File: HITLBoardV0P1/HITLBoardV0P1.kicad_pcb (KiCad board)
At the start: 2 copper layers, 199 parts, among them J2 FTSH-105-01-L-DV, U1 TMDX570LC43HDK_Connectors, U10 DAC7750IPWPR, U11 NC7SZ04P5X, U12 SN74LVC1G08DCKR, U13 NC7SZ04P5X, U14 SN74LVC1G08DCKR, U15 DAC7750IPWPR, U16 NC7SZ04P5X, U17 SN74LVC1G08DCKR, U18 DAC7750IPWPR, U19 NC7SZ04P5X, U2 LAN8650B1-E/LMX, U20 SN74LVC1G08DCKR, U21 DAC7750IPWPR, U3 LP38852MRX-ADJ/NOPB, U4 LAN8650B1-E/LMX, U5 LP38852MRX-ADJ/NOPB, U6 LAN8650B1-E/LMX, U7 LP38852MRX-ADJ/NOPB, U8 LAN8650B1-E/LMX, U9 LP38852MRX-ADJ/NOPB

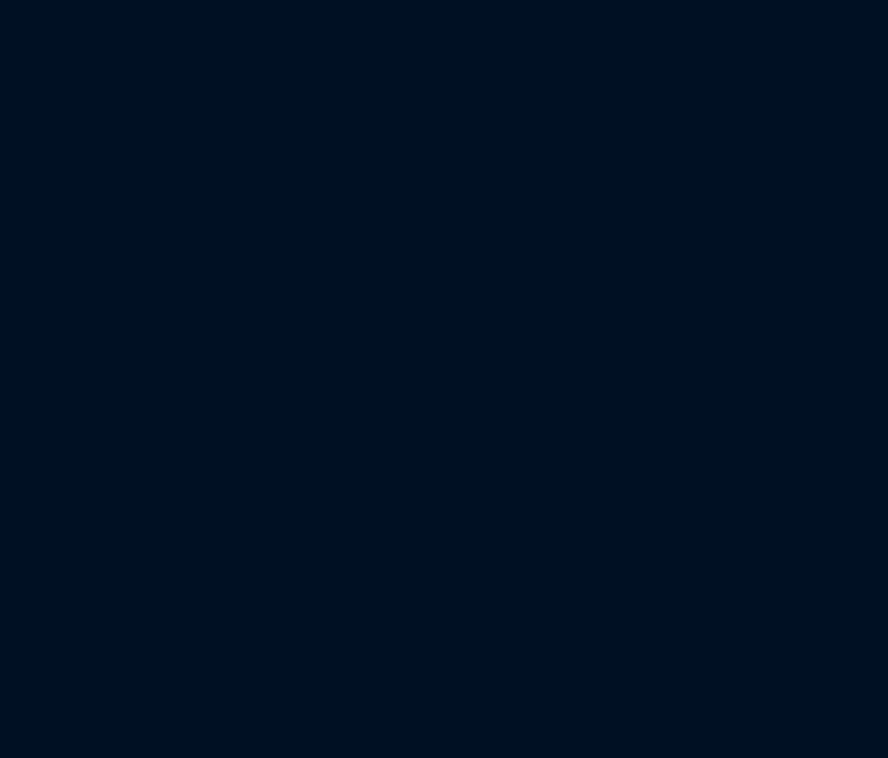
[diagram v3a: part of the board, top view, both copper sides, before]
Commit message: update to board with spi buses assigned
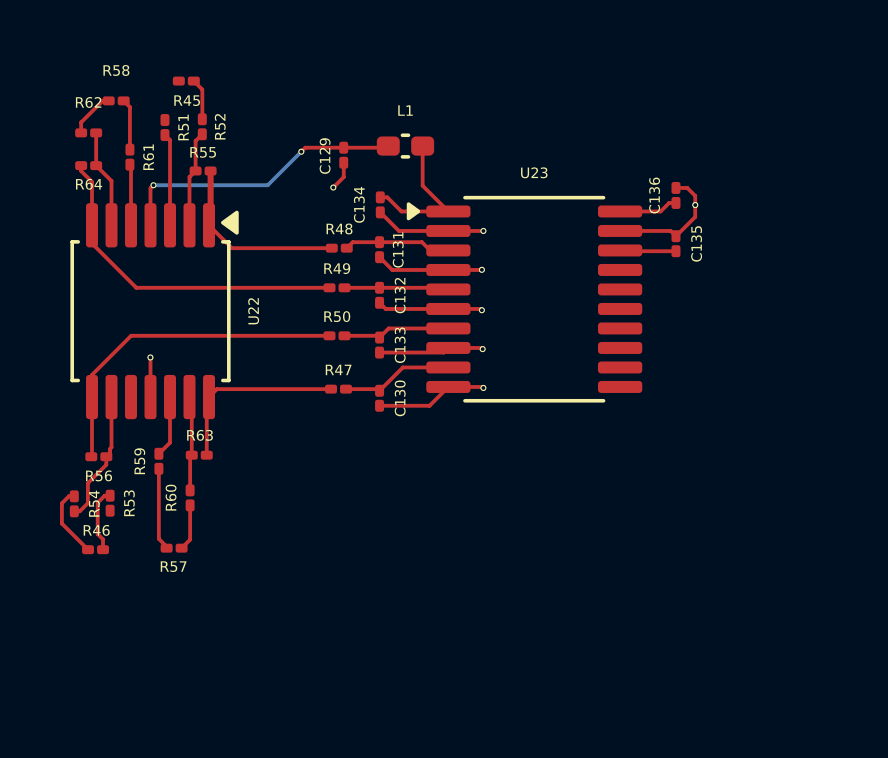
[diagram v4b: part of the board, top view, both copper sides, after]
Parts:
- added C129: C_Small, Capacitor_SMD:C_01005_0402Metric, F.Cu at (84.0, 37.9)
- added C130: C_Small, Capacitor_SMD:C_01005_0402Metric, F.Cu at (85.2, 46.0)
- added C131: C_Small, Capacitor_SMD:C_01005_0402Metric, F.Cu at (85.2, 41.0)
- added C132: C_Small, Capacitor_SMD:C_01005_0402Metric, F.Cu at (85.2, 42.5)
- added C133: C_Small, Capacitor_SMD:C_01005_0402Metric, F.Cu at (85.2, 44.2)
- added C134: C_Small, Capacitor_SMD:C_01005_0402Metric, F.Cu at (85.3, 39.5)
- added C135: C_Small, Capacitor_SMD:C_01005_0402Metric, F.Cu at (95.1, 40.8)
- added C136: C_Small, Capacitor_SMD:C_01005_0402Metric, F.Cu at (95.1, 39.2)
- added L1: L_Ferrite, Inductor_SMD:L_0402_1005Metric_Pad0.77x0.64mm_HandSolder, F.Cu at (86.1, 37.6)
- added R45: 150, Resistor_SMD:R_01005_0402Metric, F.Cu at (78.8, 35.4)
- added R46: 150, Resistor_SMD:R_01005_0402Metric, F.Cu at (75.8, 51.0)
- added R47: R_US, Resistor_SMD:R_01005_0402Metric, F.Cu at (83.9, 45.7)
- added R48: R_US, Resistor_SMD:R_01005_0402Metric, F.Cu at (83.9, 41.0)
- added R49: R_US, Resistor_SMD:R_01005_0402Metric, F.Cu at (83.8, 42.3)
- added R50: R_US, Resistor_SMD:R_01005_0402Metric, F.Cu at (83.8, 43.9)
- added R51: 1K, Resistor_SMD:R_01005_0402Metric, F.Cu at (78.1, 36.9)
- added R52: 1K, Resistor_SMD:R_01005_0402Metric, F.Cu at (79.3, 36.9)
- added R53: 100K, Resistor_SMD:R_01005_0402Metric, F.Cu at (76.3, 49.5)
- added R54: 100K, Resistor_SMD:R_01005_0402Metric, F.Cu at (75.1, 49.5)
- added R55: 1K, Resistor_SMD:R_01005_0402Metric, F.Cu at (79.4, 38.4)
- added R56: 100K, Resistor_SMD:R_01005_0402Metric, F.Cu at (75.9, 47.9)
- added R57: 150, Resistor_SMD:R_01005_0402Metric, F.Cu at (78.4, 51.0)
- added R58: 150, Resistor_SMD:R_01005_0402Metric, F.Cu at (76.5, 36.1)
- added R59: 100K, Resistor_SMD:R_01005_0402Metric, F.Cu at (77.9, 48.1)
- added R60: 100K, Resistor_SMD:R_01005_0402Metric, F.Cu at (78.9, 49.3)
- added R61: 100K, Resistor_SMD:R_01005_0402Metric, F.Cu at (76.9, 37.9)
- added R62: 100K, Resistor_SMD:R_01005_0402Metric, F.Cu at (75.5, 37.1)
- added R63: 100K, Resistor_SMD:R_01005_0402Metric, F.Cu at (79.2, 47.9)
- added R64: 100K, Resistor_SMD:R_01005_0402Metric, F.Cu at (75.5, 38.2)
- added U22: TLV4387PWR, Package_SO:TSSOP-14_4.4x5mm_P0.65mm, F.Cu at (77.6, 43.1)
- added U23: ADS131M04QPWRQ1, Package_SO:TSSOP-20_4.4x6.5mm_P0.65mm, F.Cu at (90.4, 42.7)
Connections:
- U10 pad 10: /DAC/SDO -> /RPI_SPI1_MISO
- U10 pad 6: /DAC/CLR -> /DAC_CLR0
- U10 pad 7: /DAC/LATCH -> /DAC_LATCH0
- U10 pad 9: /DAC/DIN -> /RPI_SPI1_MOSI
- U11 pad 2: /DAC/LATCH -> /DAC_LATCH0
- U12 pad 2: /DAC/SCLK -> /RPI_SPI1_SCK
- U13 pad 2: /dac2/LATCH -> /DAC_LATCH1
- U15 pad 10: /dac2/SDO -> /RPI_SPI1_MISO
- U15 pad 6: /dac2/CLR -> /DAC_CLR1
- U15 pad 7: /dac2/LATCH -> /DAC_LATCH1
- U15 pad 9: /dac2/DIN -> /RPI_SPI1_MOSI
- U16 pad 2: /dac3/LATCH -> /DAC_LATCH2
- U17 pad 2: /dac3/SCLK -> /RPI_SPI1_SCK
- U18 pad 10: /dac3/SDO -> /RPI_SPI1_MISO
- U18 pad 6: /dac3/CLR -> /DAC_CLR2
- U18 pad 7: /dac3/LATCH -> /DAC_LATCH2
- U18 pad 9: /dac3/DIN -> /RPI_SPI1_MOSI
- U19 pad 2: /dac4/LATCH -> /DAC_LATCH3
- U20 pad 2: /dac4/SCLK -> /RPI_SPI1_SCK
- U21 pad 10: /dac4/SDO -> /RPI_SPI1_MISO
- U21 pad 6: /dac4/CLR -> /DAC_CLR3
- U21 pad 7: /dac4/LATCH -> /DAC_LATCH3
- U21 pad 9: /dac4/DIN -> /RPI_SPI1_MOSI
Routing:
- net GND: track 240.0 -> 264.6 mm, vias 78 -> 86
- net /dac4/LATCH: track 20.3 -> 0.00 mm
- net /DAC_LATCH3: track 0.00 -> 20.3 mm
- net /dac2/LATCH: track 16.8 -> 0.00 mm, vias 2 -> 0
- net /DAC_LATCH1: track 0.00 -> 16.8 mm, vias 0 -> 2
- net /dac3/LATCH: track 16.0 -> 0.00 mm, vias 2 -> 0
- net /DAC_LATCH2: track 0.00 -> 16.0 mm, vias 0 -> 2
- net /DAC_LATCH0: track 0.00 -> 14.6 mm, vias 0 -> 2
- net /DAC/LATCH: track 14.6 -> 0.00 mm, vias 2 -> 0
- net /CurrentInstrument/Out_B: track 0.00 -> 11.3 mm
- net /CurrentInstrument/Out_C: track 0.00 -> 11.2 mm
- net +3V3: track 141.3 -> 151.1 mm, vias 24 -> 26
- net /CurrentInstrument/Out_A: track 0.00 -> 6.32 mm
- net /CurrentInstrument/Out_D: track 0.00 -> 6.15 mm
- net Net-(U23-AVDD): track 0.00 -> 5.00 mm
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
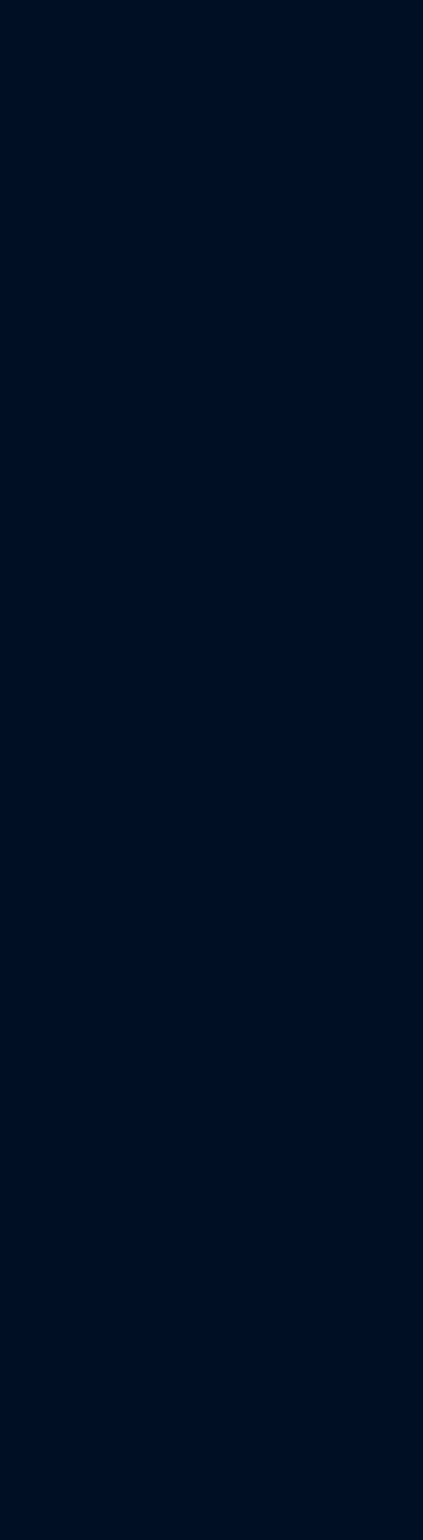
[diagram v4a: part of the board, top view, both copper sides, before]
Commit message: ADD SOLENOID VALVE CIRCUIT
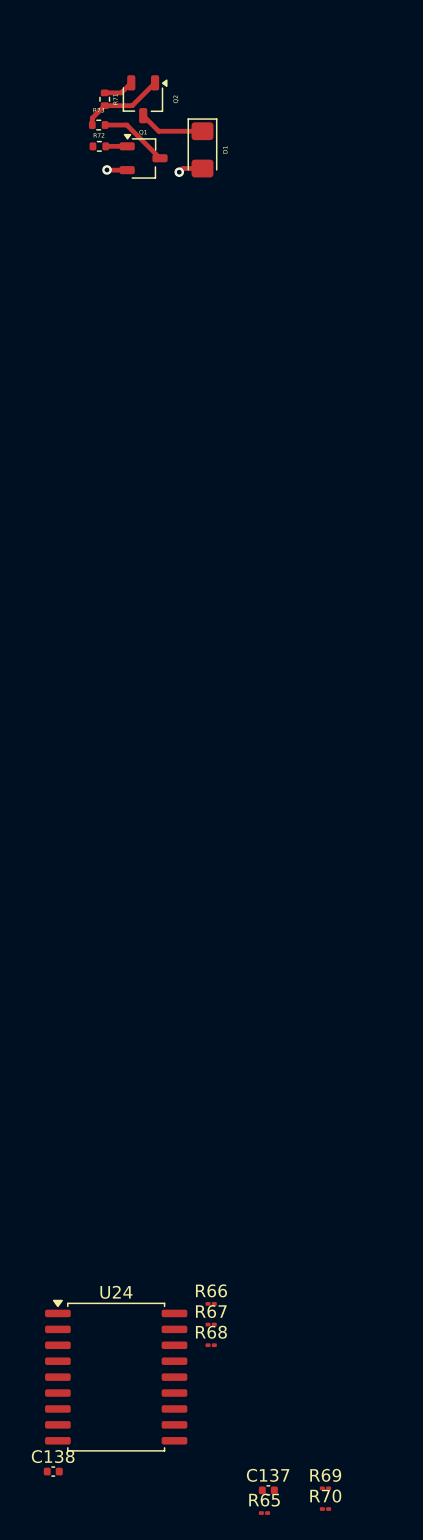
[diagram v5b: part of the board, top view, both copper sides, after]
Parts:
- added C137: 0.1u, Capacitor_SMD:C_0402_1005Metric, F.Cu at (70.6, 228.8)
- added C138: 0.1u, Capacitor_SMD:C_0402_1005Metric, F.Cu at (53.4, 227.3)
- added D1: D_Schottky, Diode_SMD:D_1206_3216Metric_Pad1.42x1.75mm_HandSolder, F.Cu at (65.3, 121.8)
- added Q1: NPN, GaladyneFootprintsLibrary:TSOT-23_KSC1623GMTF, F.Cu at (60.6, 122.5)
- added Q2: PMOS, GaladyneFootprintsLibrary:TSOT-23_ZXMP6A14FQ, F.Cu at (60.6, 117.8)
- added R65: 10K, Resistor_SMD:R_01005_0402Metric, F.Cu at (70.3, 230.6)
- added R66: 10K, Resistor_SMD:R_01005_0402Metric, F.Cu at (66.0, 213.9)
- added R67: 10K, Resistor_SMD:R_01005_0402Metric, F.Cu at (66.0, 215.6)
- added R68: 10K, Resistor_SMD:R_01005_0402Metric, F.Cu at (66.0, 217.2)
- added R69: 10K, Resistor_SMD:R_01005_0402Metric, F.Cu at (75.2, 228.6)
- added R70: 10K, Resistor_SMD:R_01005_0402Metric, F.Cu at (75.2, 230.3)
- added R71: 10K, Resistor_SMD:R_0402_1005Metric, F.Cu at (57.5, 117.8)
- added R72: 33, Resistor_SMD:R_0402_1005Metric, F.Cu at (57.1, 121.6)
- added R73: 4.7K, Resistor_SMD:R_0402_1005Metric, F.Cu at (57.1, 119.9)
- added U24: MCP23008-E/SO, Package_SO:SOIC-18W_7.5x11.6mm_P1.27mm, F.Cu at (58.5, 219.8)
- C129, C131, C132, C133, C134, C136: value C_Small -> 0.1u
- C130, C135: value C_Small -> 0.1U
- R47, R48, R49, R50: value R_US -> 500
- R51, R52: value 1K -> 100K
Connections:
- A1 pad 31: /LAN_RESET_N_1 -> /RPI_I2C_SDA
- A1 pad 32: /LAN_WAKE_0 -> /RPI_I2C_SCL
- A1 pad 34: /LAN_WAKE_1 -> /GPIO_XPNDR_IRQ
- C107 pad 1: /DAC/CURRENT_OUT -> /I_LOOP_1
- C114 pad 1: /dac2/CURRENT_OUT -> /I_LOOP_2
- C121 pad 1: /dac3/CURRENT_OUT -> /I_LOOP_3
- C128 pad 1: /dac4/CURRENT_OUT -> /I_LOOP_4
- R2 pad 1: /Ethernet/RESET_N -> /LAN1_RESET_N
- R26 pad 1: /ethernet4/RESET_N -> /LAN2_RESET_N
- R27 pad 1: /ethernet4/IRQ_N -> /LAN2_IRQ_N
- R3 pad 1: /Ethernet/IRQ_N -> /LAN1_IRQ_N
- R34 pad 2: /DAC/CURRENT_OUT -> /I_LOOP_1
- R38 pad 2: /dac2/CURRENT_OUT -> /I_LOOP_2
- R41 pad 2: /dac3/CURRENT_OUT -> /I_LOOP_3
- R44 pad 2: /dac4/CURRENT_OUT -> /I_LOOP_4
- R45 pad 2: Net-(R45-Pad2) -> /I_LOOP_1
- R46 pad 2: Net-(R46-Pad2) -> /I_LOOP_3
- R51 pad 1: Net-(R45-Pad2) -> /I_LOOP_1
- R53 pad 1: Net-(R46-Pad2) -> /I_LOOP_3
- R57 pad 2: Net-(R57-Pad2) -> /I_LOOP_4
- R58 pad 2: Net-(R58-Pad2) -> /I_LOOP_2
- R59 pad 1: Net-(R57-Pad2) -> /I_LOOP_4
- R61 pad 1: Net-(R58-Pad2) -> /I_LOOP_2
- U1 pad P11-19: /TMDX_Breakout/GIOA_1 -> /LAN1_WAKE
- U1 pad P11-21: /TMDX_Breakout/GIOA_3 -> /LAN2_WAKE
- U1 pad P11-23: /TMDX_Breakout/GIOA_5 -> /LAN1_RESET_N
- U1 pad P11-25: /TMDX_Breakout/GIOA_7 -> /LAN2_RESET_N
- U1 pad P11-27: /TMDX_Breakout/GIOB_1 -> /LAN1_IRQ_N
- U1 pad P11-29: /TMDX_Breakout/GIOB_3 -> /LAN2_IRQ_N
- U1 pad P11-5: /TMDX_Breakout/SCI1_RX -> /RPI_UART1_TX
- U1 pad P11-6: /TMDX_Breakout/SCI1_TX -> /RPI_UART1_RX
- U1 pad P9-11: /TMDX_Breakout/SPI1_SIMO -> /TMDX_SPI1_SIMO
- U1 pad P9-12: /TMDX_Breakout/SPI1_SOMI -> /TMDX_SPI1_SOMI
- U1 pad P9-16: unconnected-(U1A-SPI5_CLK-PadP9-16) -> /TMDX_Breakout/SPI5_SCLK
- U1 pad P9-17: unconnected-(U1A-SPI5_CS1_N-PadP9-17) -> /TMDX_Breakout/SPI5_CS1_NR
- U1 pad P9-18: unconnected-(U1A-SPI5_CS0_N-PadP9-18) -> /TMDX_Breakout/SPI5_CS0_N
- U1 pad P9-21: unconnected-(U1A-SPI5_SIMO_0-PadP9-21) -> /TMDX_Breakout/SPI5_SIMO_0
- U1 pad P9-22: unconnected-(U1A-SPI5_SOMI_0-PadP9-22) -> /TMDX_Breakout/SPI5_SOMI_0
- U1 pad P9-6: /TMDX_Breakout/SPI1_CLK -> /TMDX_SPI1_SCLK
- U1 pad P9-7: /TMDX_Breakout/SPI1_CS1 -> /TMDX_SPI1_CS1
- U1 pad P9-8: /TMDX_Breakout/SPI1_CS0_N -> /TMDX_SPI1_CS0_N
- U2 pad 10: /Ethernet/SPI_SDO -> /TMDX_SPI1_SOMI
- U2 pad 11: /Ethernet/SPI_CS_N -> /TMDX_SPI1_CS0_N
- U2 pad 12: /Ethernet/SPI_SCLK -> /TMDX_SPI1_SCLK
- U2 pad 13: /Ethernet/SPI_SDI -> /TMDX_SPI1_SIMO
- U2 pad 32: /Ethernet/WAKE_IN_3V3 -> /LAN1_WAKE
- U2 pad 8: /Ethernet/RESET_N -> /LAN1_RESET_N
- U2 pad 9: /Ethernet/IRQ_N -> /LAN1_IRQ_N
- U23 pad 12: unconnected-(U23-CHIP_SELECT_N-Pad12) -> /ADC_CS_N
- U23 pad 13: unconnected-(U23-DATA_READY_N-Pad13) -> /ADC_DRDY
- U23 pad 14: unconnected-(U23-SCLK-Pad14) -> /CurrentInstrument/SCLK
- U23 pad 15: unconnected-(U23-DOUT-Pad15) -> /CurrentInstrument/SDO
- U23 pad 16: unconnected-(U23-DIN-Pad16) -> /CurrentInstrument/SDI
- U8 pad 10: /ethernet4/SPI_SDO -> /TMDX_SPI1_SOMI
- U8 pad 11: /ethernet4/SPI_CS_N -> /TMDX_SPI1_CS1
- U8 pad 12: /ethernet4/SPI_SCLK -> /TMDX_SPI1_SCLK
- U8 pad 13: /ethernet4/SPI_SDI -> /TMDX_SPI1_SIMO
- U8 pad 32: /ethernet4/WAKE_IN_3V3 -> /LAN2_WAKE
- U8 pad 8: /ethernet4/RESET_N -> /LAN2_RESET_N
- U8 pad 9: /ethernet4/IRQ_N -> /LAN2_IRQ_N
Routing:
- net /ethernet4/RESET_N: track 6.74 -> 0.00 mm
- net /LAN2_RESET_N: track 0.00 -> 6.74 mm
- net Net-(Q2-G): track 0.00 -> 6.73 mm
- net Net-(Q1-C): track 0.00 -> 5.48 mm
- net /Solenoid-Valve/SV_24VDC_OUT: track 0.00 -> 5.24 mm
- net /I_LOOP_4: track 0.00 -> 5.22 mm
- net /I_LOOP_3: track 0.00 -> 4.70 mm
- net /Ethernet/RESET_N: track 4.67 -> 0.00 mm
- net /Ethernet/1V8_U2: track 26.7 -> 31.4 mm
- net /I_LOOP_2: track 0.00 -> 4.31 mm
- net /Ethernet/U3_ADJ: track 3.68 -> 7.39 mm
- net /Ethernet/IRQ_N: track 3.71 -> 0.00 mm
- net GND: track 264.6 -> 268.2 mm, vias 86 -> 88
- net Net-(R57-Pad2): track 2.75 -> 0.00 mm
- net /I_LOOP_1: track 0.00 -> 2.62 mm
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
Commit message: update solenoid valve circuits
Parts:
- added D2: LED, LED_SMD:LED_01005_0402Metric, F.Cu at (69.0, 123.5)
- added D3: D_Schottky, Diode_SMD:D_1206_3216Metric_Pad1.42x1.75mm_HandSolder, F.Cu at (59.4, 178.5)
- added D4: LED, LED_SMD:LED_01005_0402Metric, F.Cu at (62.8, 179.1)
- added Q3: NPN, GaladyneFootprintsLibrary:TSOT-23_KSC1623GMTF, F.Cu at (55.4, 185.4)
- added Q4: PMOS, GaladyneFootprintsLibrary:TSOT-23_ZXMP6A14FQ, F.Cu at (53.8, 178.3)
- added R74: 500, Resistor_SMD:R_01005_0402Metric, F.Cu at (69.0, 120.3)
- added R75: 10K, Resistor_SMD:R_01005_0402Metric, F.Cu at (67.2, 120.3)
- added R76: 3500, Resistor_SMD:R_01005_0402Metric, F.Cu at (67.2, 123.5)
- added R77: 10K, Resistor_SMD:R_0402_1005Metric, F.Cu at (51.9, 182.2)
- added R78: 33, Resistor_SMD:R_0402_1005Metric, F.Cu at (51.6, 185.0)
- added R79: 4.7K, Resistor_SMD:R_0402_1005Metric, F.Cu at (56.2, 182.1)
- added R80: 500, Resistor_SMD:R_01005_0402Metric, F.Cu at (62.8, 177.3)
- added R81: 10K, Resistor_SMD:R_01005_0402Metric, F.Cu at (64.8, 177.3)
- added R82: 3500, Resistor_SMD:R_01005_0402Metric, F.Cu at (64.8, 179.1)
- moved D1 1.07 mm to (64.3, 122.0)
- moved Q2 1.07 mm to (59.6, 118.0)
- moved R73 1.07 mm to (56.0, 120.0)
- moved Q1 1.07 mm to (59.6, 122.7)
- moved R72 1.07 mm to (56.1, 121.7)
- moved R71 1.07 mm to (56.5, 118.0)
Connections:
- Q2 pad 3: /Solenoid-Valve/24VDC -> +12V
- R71 pad 1: /Solenoid-Valve/24VDC -> +12V
- R72 pad 1: /Solenoid-Valve/SV_EN_3V3 -> /SV_EN_1
- U1 pad P11-31: /TMDX_Breakout/GIOB_5 -> /SV_EN_1
- U24 pad 13: /I2C_GPIO_EXPANDER/GP3 -> /SV_ON_1
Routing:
- net /Solenoid-Valve1/SV_24VDC_OUT: track 0.00 -> 11.0 mm
- net GND: track 268.2 -> 278.1 mm, vias 88 -> 92
- net Net-(Q4-G): track 0.00 -> 6.07 mm
- net +12V: track 20.8 -> 26.6 mm, vias 0 -> 2
- net /Solenoid-Valve/SV_24VDC_OUT: track 5.24 -> 10.1 mm
- net /SV_ON_1: track 0.00 -> 3.97 mm
- net Net-(Q3-C): track 0.00 -> 3.26 mm
- net Net-(D2-A): track 0.00 -> 2.66 mm
- net Net-(Q3-B): track 0.00 -> 2.49 mm
- net /Solenoid-Valve/24VDC: track 2.45 -> 0.00 mm
- net Net-(D4-A): track 0.00 -> 1.29 mm

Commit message: add reset button groups
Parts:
- added D5: LED, LED_SMD:LED_01005_0402Metric, F.Cu at (513.6, 197.5)
- added D6: LED, LED_SMD:LED_01005_0402Metric, F.Cu at (513.6, 199.2)
- added D7: LED, LED_SMD:LED_01005_0402Metric, F.Cu at (513.6, 200.8)
- added R83: 10K, Resistor_SMD:R_01005_0402Metric, F.Cu at (487.5, 197.4)
- added R84: 10K, Resistor_SMD:R_01005_0402Metric, F.Cu at (490.2, 204.6)
- added R85: 75, Resistor_SMD:R_0402_1005Metric, F.Cu at (510.8, 197.7)
- added R86: 75, Resistor_SMD:R_0402_1005Metric, F.Cu at (510.8, 199.7)
- added R87: 75, Resistor_SMD:R_0402_1005Metric, F.Cu at (510.8, 201.7)
- added SW1: SW_Push, Button_Switch_SMD:SW_Push_1P1T_NO_E-Switch_TL3301NxxxxxG, F.Cu at (470.8, 177.8)
- added SW2: SW_Push, Button_Switch_SMD:SW_Push_1P1T_NO_E-Switch_TL3301NxxxxxG, F.Cu at (501.2, 200.5)
- moved C93 301.0 mm to (92.4, 152.6), turned to 90 degrees
- moved C90 299.3 mm to (94.2, 152.6), turned to 90 degrees
- moved C87 297.7 mm to (96.0, 152.5), turned to 90 degrees
- moved C86 296.1 mm to (97.7, 152.5), turned to 90 degrees
- moved R29 293.2 mm to (90.7, 161.7), turned to 180 degrees
- moved U9 292.2 mm to (95.0, 158.6), turned to 90 degrees
- moved R28 291.2 mm to (90.7, 163.7), turned to 180 degrees
- moved C97 290.7 mm to (99.2, 156.3), turned to -90 degrees
- moved C100 288.0 mm to (93.7, 163.9), turned to 180 degrees
- moved C78 286.6 mm to (100.4, 159.1), turned to 90 degrees
- moved C99 286.0 mm to (93.7, 165.9), turned to 180 degrees
- moved C94 285.4 mm to (96.4, 163.9), turned to 0 degrees
- moved C79 284.8 mm to (102.4, 159.1), turned to 90 degrees
- moved C76 284.0 mm to (105.2, 157.4), turned to 90 degrees
- moved C77 282.2 mm to (107.2, 157.4), turned to 90 degrees
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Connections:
- A1 pad 30: /RaspberryPiPico/RESET_N -> /RESET_N
- A1 pad TP6: unconnected-(A1-~{BOOTSEL}-PadTP6) -> /RaspberryPiPico/BOOTSEL_N
- J2 pad 10: /RaspberryPiPico/RESET_N -> /RESET_N
- R78 pad 1: /SV_EN_1 -> /SV_EN_2
- R81 pad 1: /SV_ON_1 -> /SV_ON_2
- R82 pad 2: /SV_ON_1 -> /SV_ON_2
- U1 pad P11-33: unconnected-(U1C-GIOB_7-PadP11-33) -> /SV_EN_2
- U1 pad P9-60: unconnected-(U1A-POR_RST_N-PadP9-60) -> /RESET_N
- U24 pad 14: /I2C_GPIO_EXPANDER/GP4 -> /SV_ON_2
- U24 pad 15: /I2C_GPIO_EXPANDER/GP5 -> /LED0
- U24 pad 16: /I2C_GPIO_EXPANDER/GP6 -> /LED1
- U24 pad 17: /I2C_GPIO_EXPANDER/GP7 -> /LED2
- U24 pad 6: /I2C_GPIO_EXPANDER/RESET_N -> /RESET_N
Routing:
- net /SV_ON_2: track 0.00 -> 1.30 mm
- net /SV_ON_1: track 3.97 -> 2.67 mm
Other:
- board text added: "RESET"
- board text added: "RPI BOOTSEL"

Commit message: MINOR UPDATES -- SWTICH ONE LAN TO SPI 5 INSTEAD OF SPI1 ON THE TMDX, SET UP LAN8650S for actual differential pair routing by changing suffix to "_DN" and "_DP" instead of "_N" or "_P" or just "N", "P"
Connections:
- net /Ethernet/ETH_10T1S_TRXN renamed /Ethernet/ETH_10T1S_TRX_DN
- net /Ethernet/ETH_10T1S_TRXP renamed /Ethernet/ETH_10T1S_TRX_DP
- net /Ethernet/TRXN renamed /Ethernet/TRX_DN
- net /Ethernet/TRXP renamed /Ethernet/TRX_DP
- net /Ethernet2/TRXN renamed /Ethernet2/TRX_DN
- net /Ethernet2/TRXP renamed /Ethernet2/TRX_DP
- net /ethernet3/TRXN renamed /ethernet3/TRX_DN
- net /ethernet3/TRXP renamed /ethernet3/TRX_DP
- net /ethernet4/TRXN renamed /ethernet4/TRX_DN
- net /ethernet4/TRXP renamed /ethernet4/TRX_DP
- R10 pad 1: /LAN_RESET_N_1 -> /RESET_N
- R18 pad 1: /LAN_RESET_N_0 -> /RESET_N
- R2 pad 1: /LAN1_RESET_N -> /RESET_N
- R26 pad 1: /LAN2_RESET_N -> /RESET_N
- U1 pad P11-23: /LAN1_RESET_N -> /TMDX_Breakout/GIOA_5
- U1 pad P11-25: /LAN2_RESET_N -> /TMDX_Breakout/GIOA_7
- U2 pad 8: /LAN1_RESET_N -> /RESET_N
- U24 pad 10: /LAN_RESET_N_1 -> /I2C_GPIO_EXPANDER/GP0
- U4 pad 8: /LAN_RESET_N_1 -> /RESET_N
- U6 pad 8: /LAN_RESET_N_0 -> /RESET_N
- U8 pad 8: /LAN2_RESET_N -> /RESET_N
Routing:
- net (no net): track 27.8 -> 1.73 mm
- net /RESET_N: track 0.00 -> 19.6 mm
- net GND: track 278.1 -> 290.1 mm
- net Net-(C23-Pad2): track 1.68 -> 10.3 mm
- net /LAN_RESET_N_1: track 6.87 -> 0.00 mm
- net /LAN2_RESET_N: track 6.74 -> 0.00 mm
- net /LAN_RESET_N_0: track 5.95 -> 0.00 mm
- net /Ethernet/1V8_U2: track 31.4 -> 36.8 mm
